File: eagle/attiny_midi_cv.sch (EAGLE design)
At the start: 26 parts, among them IC1 TL072P, Q518 2N3904, U2 TINY45-20-DIP

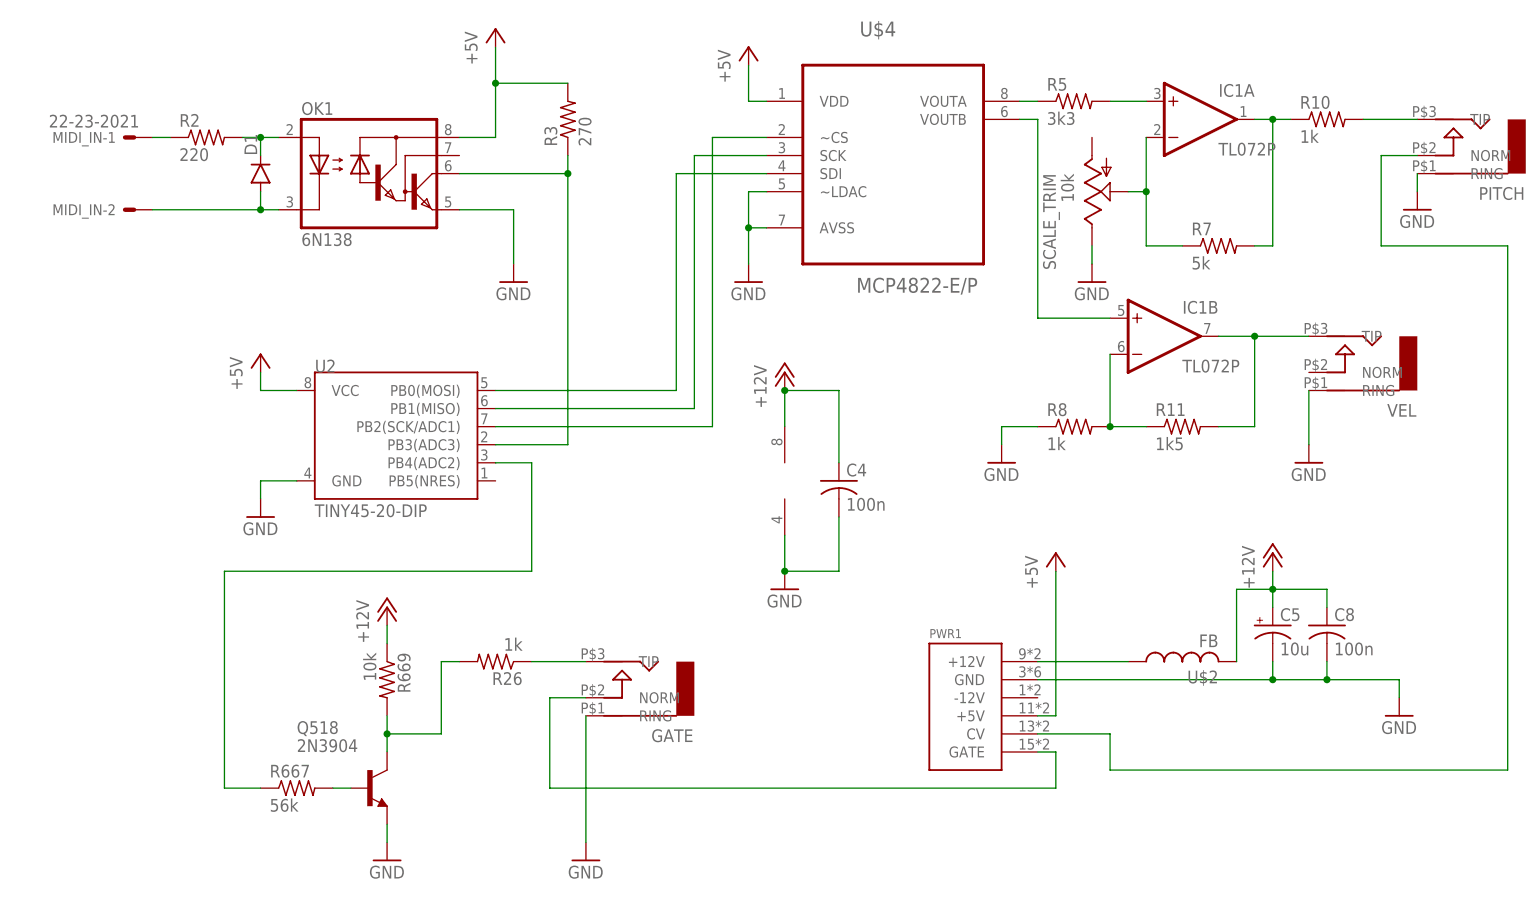
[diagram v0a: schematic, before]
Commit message: fixed brd and getting channel from eeprom
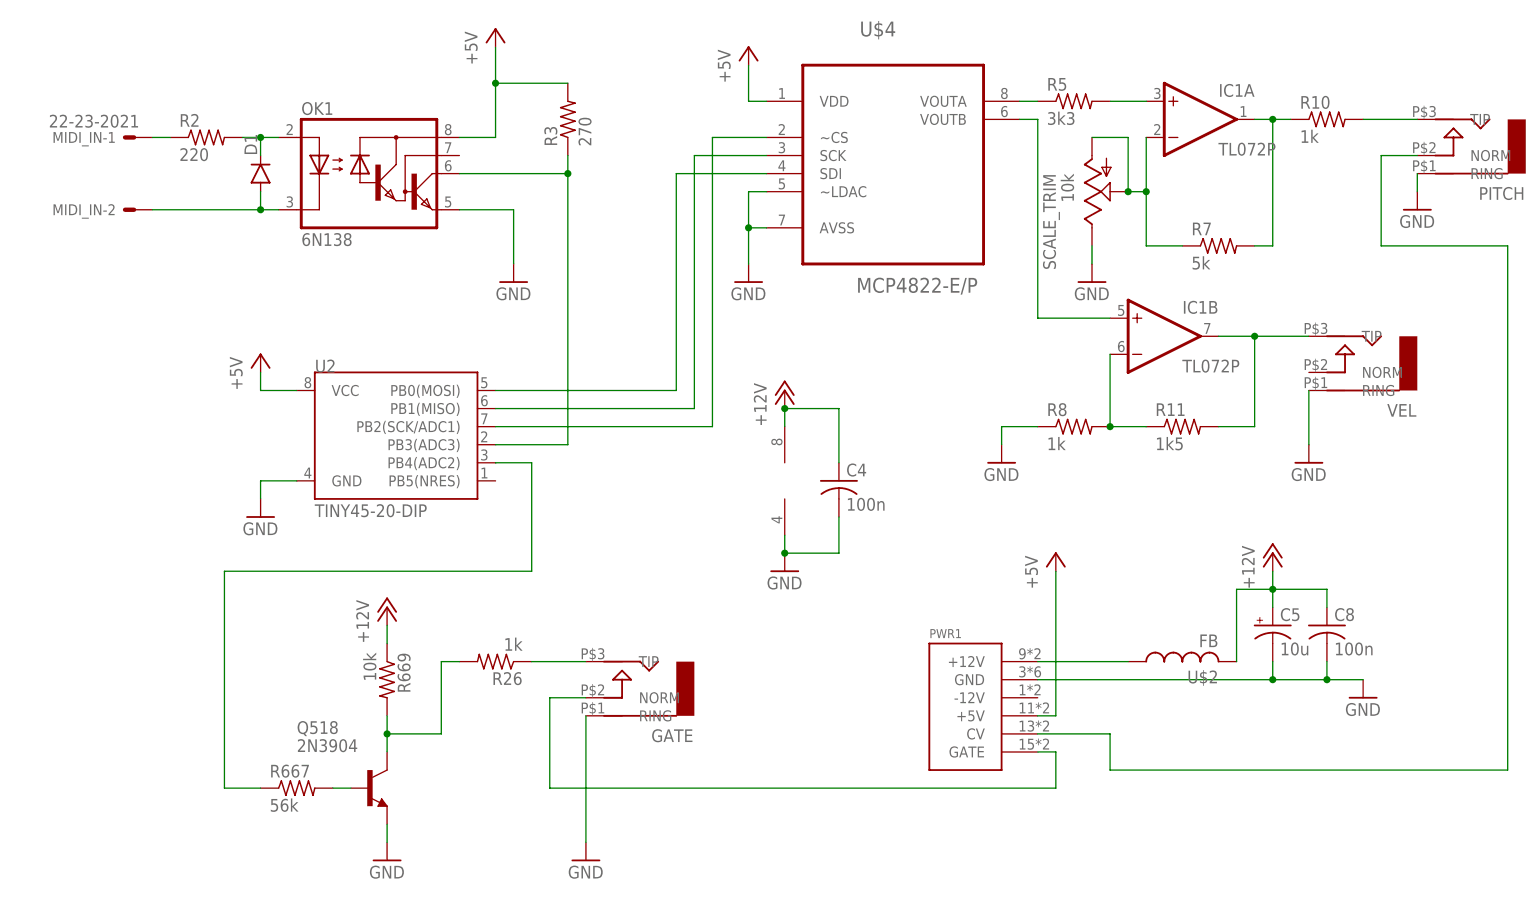
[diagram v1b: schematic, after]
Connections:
- removed net N$10: C4.2, C5.-, C8.2, GATE.RING, IC1P.V-, OK1.GND, PITCH.RING, PWR1.GND, R8.1, SCALE_TRIM.E, U$4.AVSS, U$4.~LDAC, VEL.RING
- net GND: now also C4.2, C5.-, C8.2, GATE.RING, IC1P.V-, OK1.GND, PITCH.RING, PWR1.GND, R8.1, SCALE_TRIM.E, U$4.AVSS, U$4.~LDAC, VEL.RING
- net N$12: now also SCALE_TRIM.A

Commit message: schematic has thru and back to softwareserial
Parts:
- added MIDI_OUT_THRU1: 22-23-2031, con-molex:22-23-2031
- added R1, R4: 220, rcl:R-US_0207/7
- R26: device rcl:R-US_0309/12 -> rcl:R-US_0309/10
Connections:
- new net N$10: MIDI_OUT_THRU1-2.S, R4.2
- new net N$16: R4.1, U2.PB5(NRES)
- new net N$9: MIDI_OUT_THRU1-1.S, R1.2
- net +5V: now also R1.1
- net GND: now also MIDI_OUT_THRU1-3.S
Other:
- moved on the sheet: C4, MIDI_IN-1
